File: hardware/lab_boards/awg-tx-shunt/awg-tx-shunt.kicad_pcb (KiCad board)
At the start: 2 copper layers, 66 x 57.1 mm, 12 parts, among them J1 FROM PWR AMP, J2 TX, J3 SHUNT

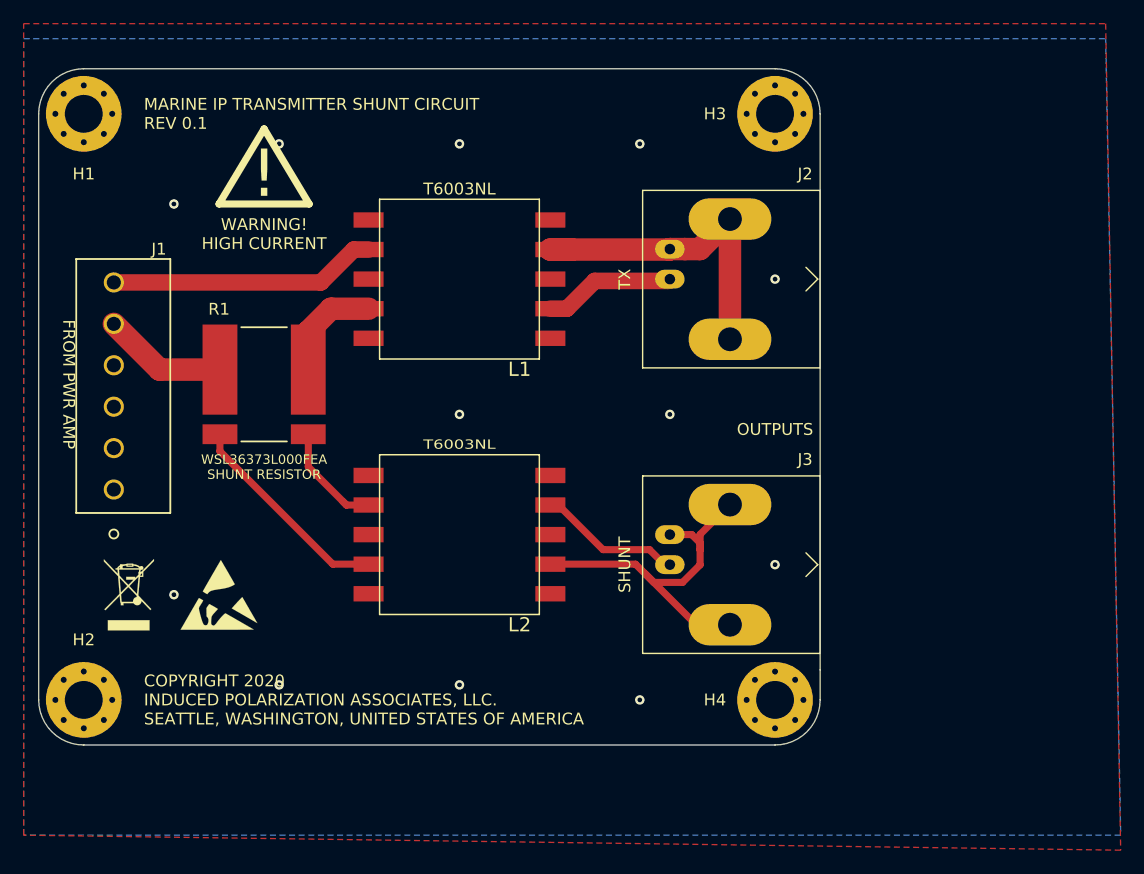
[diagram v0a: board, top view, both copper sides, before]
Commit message: Added two DPDT switches to the board and rerouted to avoid using the bottom layer grounding plane.
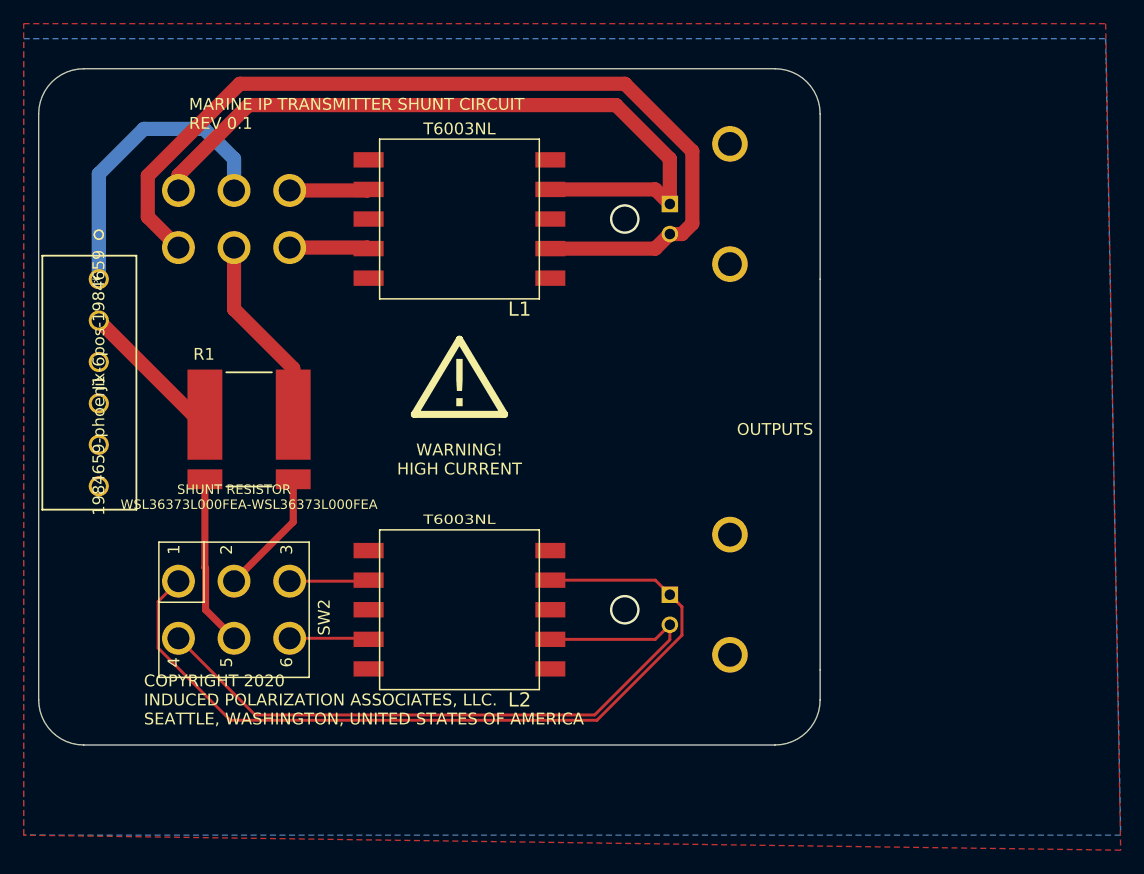
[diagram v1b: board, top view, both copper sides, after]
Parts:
- removed H1, H2, H3, H4: MountingHole, MountingHole:MountingHole_3.2mm_M3_Pad_Via
- removed REF**: ESD-Logo_6.6x6mm_SilkScreen, Symbol:ESD-Logo_6.6x6mm_SilkScreen
- removed REF**: WEEE-Logo_4.2x6mm_SilkScreen, Symbol:WEEE-Logo_4.2x6mm_SilkScreen
- added SW1: 100DP1T1B1M2QEH, switches:100DP1T1B1M2QEH, B.Cu at (92.7, 88.9)
- added SW2: 100DP1T1B1M2QEH, switches:100DP1T1B1M2QEH, F.Cu at (92.7, 121.9)
- J1: value FROM PWR AMP -> 1984659-phoenix-6pos-1984659; footprint phoenix-6pos-1984659:1984659 -> phoenix-6-pos-1984659:1984659
- J2: value TX -> TX OUT; footprint Connector_Coaxial:BNC_Amphenol_B6252HB-NPP3G-50_Horizontal -> amphenol-isolated-pcb-mount-bnc:CONN_1-1337543-0; moved to B.Cu
- J3: value SHUNT -> TX-SHUNT; footprint Connector_Coaxial:BNC_Amphenol_B6252HB-NPP3G-50_Horizontal -> amphenol-isolated-pcb-mount-bnc:CONN_1-1337543-0; moved to B.Cu
- R1: value WSL36373L000FEA -> WSL36373L000FEA-WSL36373L000FEA
- moved J1 17.8 mm to (81.3, 94.0), turned to 270 degrees
- moved J2 6.35 mm to (129.5, 87.6), turned to 180 degrees
- moved L2 6.35 mm to (111.8, 121.9)
- moved L1 5.08 mm to (111.8, 88.9)
- moved R1 4.02 mm to (94.0, 106.7)
- moved J3 2.54 mm to (129.5, 120.7), turned to 180 degrees
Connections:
- net Net-(J3-Pad1) renamed /SHUNTP-DIRECT
- net Net-(J3-Pad2) renamed /SHUNTN-DIRECT
- J1 pad 1: GNDPWR -> /TXP-IN
- J1 pad 2: GNDPWR -> /TXN-IN
- J1 pad 5: /TX2 -> GNDPWR
- J1 pad 6: /TX1 -> GNDPWR
- J2 pad 1: Net-(J2-Pad1) -> /TXP-DIRECT
- J2 pad 2: Net-(J2-Pad2) -> /TXN-DIRECT
- L1 pad P$2: /TX1 -> /TXP-ISO
- L1 pad P$4: Net-(L1-PadP$4) -> /TXN-ISO
- L1 pad P$7: Net-(J2-Pad1) -> /TXN-DIRECT
- L1 pad P$9: Net-(J2-Pad2) -> /TXP-DIRECT
- L2 pad P$2: /SHUNT_N -> /SHUNTP-ISO
- L2 pad P$4: /SHUNT_P -> /SHUNTN-ISO
- R1 pad 1: Net-(L1-PadP$4) -> /TXN-IN2
- R1 pad 2: /SHUNT_N -> /TXSP-IN
- R1 pad 3: /SHUNT_P -> /TXSN-IN
- R1 pad 4: /TX2 -> /TXN-IN
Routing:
- net /TXN-DIRECT: track 0.00 -> 77.7 mm
- net /TXP-DIRECT: track 0.00 -> 61.6 mm
- net /SHUNTP-DIRECT: track 12.5 -> 70.6 mm
- net Net-(J2-Pad2): track 28.3 -> 0.00 mm
- net /TXP-IN: track 0.00 -> 25.6 mm
- net /SHUNTN-DIRECT: track 35.6 -> 58.7 mm
- net /TX1: track 22.7 -> 0.00 mm
- net /SHUNT_P: track 18.0 -> 0.00 mm
- net /TXN-IN2: track 0.00 -> 16.2 mm
- net /TXSN-IN: track 0.00 -> 14.5 mm
- net /TXN-IN: track 0.00 -> 12.3 mm
- net Net-(J2-Pad1): track 11.1 -> 0.00 mm
- net /TXSP-IN: track 0.00 -> 10.7 mm
- net /TX2: track 10.6 -> 0.00 mm
- net /SHUNT_N: track 9.61 -> 0.00 mm
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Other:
- net class shunt: clearance 0.4 -> 0.6
- net class sigpwr: clearance 0.4 -> 0.6; trace_width 1.4 -> 1.2

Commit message: Added some notes to the shunt board design.
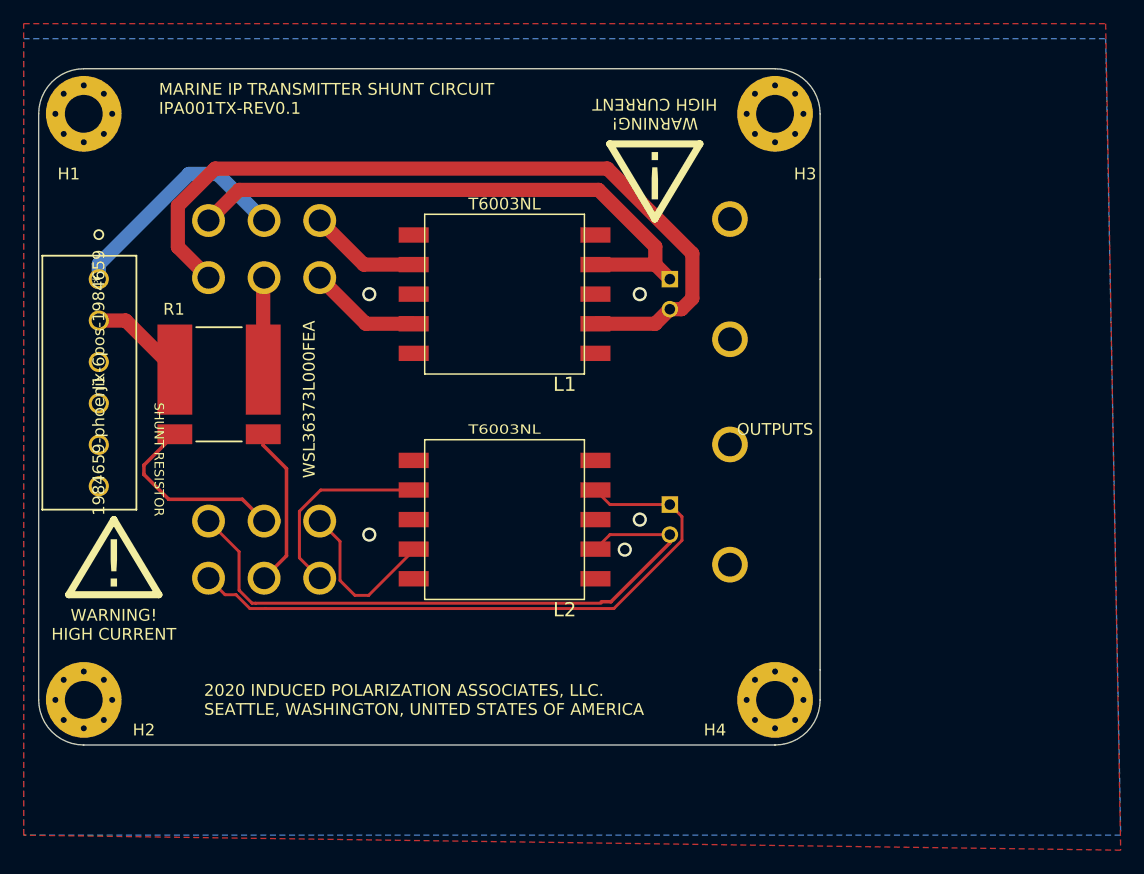
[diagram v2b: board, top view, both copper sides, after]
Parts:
- added H1: MountingHole, MountingHole:MountingHole_3.2mm_M3_Pad_Via, F.Cu at (80.0, 80.0)
- added H2: MountingHole, MountingHole:MountingHole_3.2mm_M3_Pad_Via, F.Cu at (80.0, 129.5)
- added H3: MountingHole, MountingHole:MountingHole_3.2mm_M3_Pad_Via, F.Cu at (138.4, 80.0)
- added H4: MountingHole, MountingHole:MountingHole_3.2mm_M3_Pad_Via, F.Cu at (138.4, 129.5)
- SW2: moved to B.Cu
- moved L2 8.52 mm to (115.6, 114.3)
- moved J3 7.62 mm to (129.5, 113.0)
- moved L1 7.41 mm to (115.6, 95.2)
- moved J2 6.35 mm to (129.5, 94.0)
- moved SW2 5.68 mm to (95.2, 116.8), turned to 90 degrees
- moved R1 4.58 mm to (91.4, 102.9)
- moved SW1 3.59 mm to (95.2, 91.4)
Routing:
- net /SHUNTP-DIRECT: track 70.6 -> 53.7 mm
- net /TXP-DIRECT: track 61.6 -> 49.1 mm
- net /SHUNTP-ISO: track 6.71 -> 16.8 mm
- net /TXN-DIRECT: track 77.7 -> 67.8 mm
- net /TXN-IN2: track 16.2 -> 7.80 mm
- net /SHUNTN-ISO: track 6.71 -> 14.2 mm
- net /TXP-IN: track 25.6 -> 20.0 mm
- net /SHUNTN-DIRECT: track 58.7 -> 53.3 mm
- net /TXN-IN: track 12.3 -> 8.14 mm
- net /TXSN-IN: track 14.5 -> 17.5 mm
- net /TXSP-IN: track 10.7 -> 13.8 mm
- net /TXN-ISO: track 6.71 -> 9.56 mm
- net /TXP-ISO: track 6.71 -> 9.48 mm
- net GNDPWR: vias 2 -> 5
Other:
- net class shunt: clearance 0.6 -> 0.3; trace_width 0.6 -> 0.3; via_dia 1.2 -> 0.8; via_drill 0.8 -> 0.4
- board text added: "2020 INDUCED POLARIZATION ASSOCIATES, LLC. SEATTLE, WASHINGTON, UNITED STATES OF AMERICA"
- board text added: "MARINE IP TRANSMITTER SHUNT CIRCUIT IPA001TX-REV0.1"
- board text removed: "COPYRIGHT 2020 INDUCED POLARIZATION ASSOCIATES, LLC. SEATTLE, WASHINGTON, UNITED STATES OF AMERICA"
- board text removed: "MARINE IP TRANSMITTER SHUNT CIRCUIT REV 0.1"
